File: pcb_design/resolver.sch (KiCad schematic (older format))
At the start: 37 parts, among them U15 AD2S1205, U18 SN74LVC1G, U19 AD8397, U20 APX809, U21 NCV78Mxx, X1 ABM3B - 8MHz

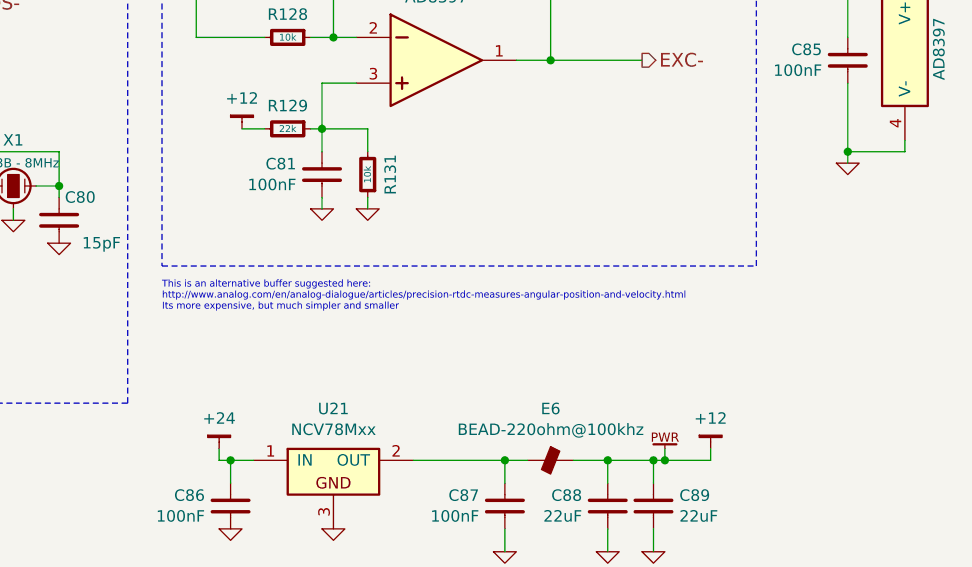
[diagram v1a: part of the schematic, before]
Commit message: Added RC filter to FAULT line to prevent noise triggering it
Signed-off-by: Marcos Chaparro <mchaparro@paltatech.com>
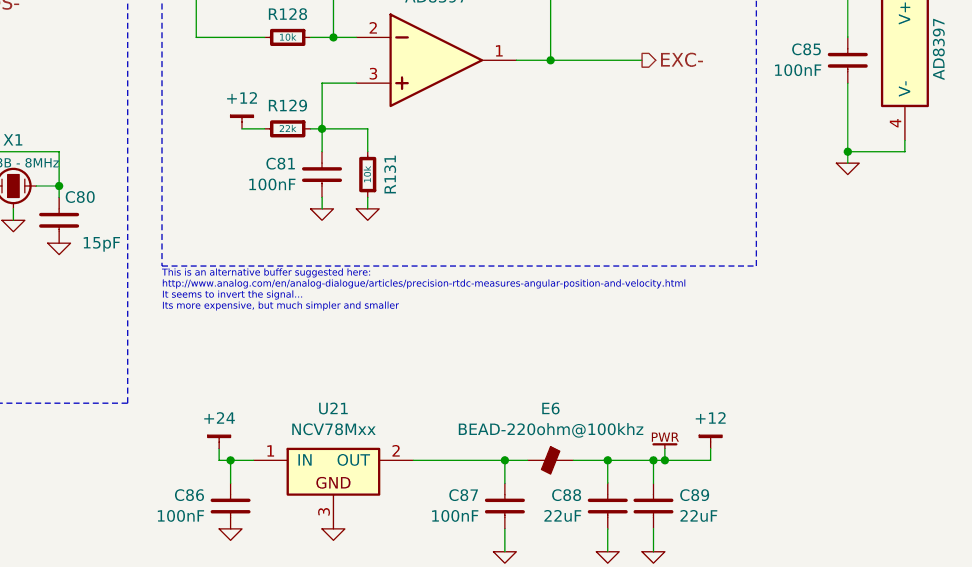
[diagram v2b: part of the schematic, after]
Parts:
- C73, C74, C75, C77, C81, C82, C85, C86, C87: BOM CAP MLCC 100pF C0G 50V 5% [0603] -> CAP MLCC 100nF C0G 50V 5% [0603]
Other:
- note added: "This is an alternative buffer suggested here:\nhttp://www.analog.com/en/analog-dialogue/articles/precision-rtdc-measures-angular-position-and-velocity.html\nIt seems to invert the signal...\nIts more expensive, but much simpler and smaller"
- note removed: "This is an alternative buffer suggested here:\nhttp://www.analog.com/en/analog-dialogue/articles/precision-rtdc-measures-angular-position-and-velocity.html\nIts more expensive, but much simpler and smaller"
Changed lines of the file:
@@
 $Descr A4 11693 8268
 encoding utf-8
-Sheet 14 15
+Sheet 12 15
 Title ""
 Date "2017-02-22"
@@
 F 2 "IPC7351-Nominal:CAPC1608X55" H -50 -550 50  0001 C CNN
 F 3 "http://www.murata.com/~/media/webrenewal/support/library/catalog/products/capacitor/mlcc/c02e.ashx" H -60 -575 60  0001 C CNN
-F 4 "CAP MLCC 100pF C0G 50V 5% [0603]" H 750 0   60  0001 C CNN "BOM"
+F 4 "CAP MLCC 100nF C0G 50V 5% [0603]" H 750 0   60  0001 C CNN "BOM"
 F 5 "Murata Electronics North America" H 0   0   50  0001 C CNN "MFR"
 F 6 "GRM188R71E104KA01D" H 0   0   50  0001 C CNN "MPN"
@@
 F 2 "IPC7351-Nominal:CAPC1608X55" H -250 -550 50  0001 C CNN
 F 3 "http://www.murata.com/~/media/webrenewal/support/library/catalog/products/capacitor/mlcc/c02e.ashx" H -260 -575 60  0001 C CNN
-F 4 "CAP MLCC 100pF C0G 50V 5% [0603]" H 550 0   60  0001 C CNN "BOM"
+F 4 "CAP MLCC 100nF C0G 50V 5% [0603]" H 550 0   60  0001 C CNN "BOM"
 F 5 "Murata Electronics North America" H 0   0   50  0001 C CNN "MFR"
 F 6 "GRM188R71E104KA01D" H 0   0   50  0001 C CNN "MPN"
@@
 F 2 "IPC7351-Nominal:CAPC1608X55" H 1100 -400 50  0001 C CNN
 F 3 "http://www.murata.com/~/media/webrenewal/support/library/catalog/products/capacitor/mlcc/c02e.ashx" H 1090 -425 60  0001 C CNN
-F 4 "CAP MLCC 100pF C0G 50V 5% [0603]" H 1900 150 60  0001 C CNN "BOM"
+F 4 "CAP MLCC 100nF C0G 50V 5% [0603]" H 1900 150 60  0001 C CNN "BOM"
 F 5 "Murata Electronics North America" H 0   0   50  0001 C CNN "MFR"
 F 6 "GRM188R71E104KA01D" H 0   0   50  0001 C CNN "MPN"
@@
 F 2 "IPC7351-Nominal:CAPC1608X55" H 4000 500 50  0001 C CNN
 F 3 "http://www.murata.com/~/media/webrenewal/support/library/catalog/products/capacitor/mlcc/c02e.ashx" H 3990 475 60  0001 C CNN
-F 4 "CAP MLCC 100pF C0G 50V 5% [0603]" H 4800 1050 60  0001 C CNN "BOM"
+F 4 "CAP MLCC 100nF C0G 50V 5% [0603]" H 4800 1050 60  0001 C CNN "BOM"
 F 5 "Murata Electronics North America" H 0   0   50  0001 C CNN "MFR"
 F 6 "GRM188R71E104KA01D" H 0   0   50  0001 C CNN "MPN"
@@
 F 2 "IPC7351-Nominal:CAPC1608X55" H 3800 2250 50  0001 C CNN
 F 3 "http://www.murata.com/~/media/webrenewal/support/library/catalog/products/capacitor/mlcc/c02e.ashx" H 3790 2225 60  0001 C CNN
-F 4 "CAP MLCC 100pF C0G 50V 5% [0603]" H 4600 2800 60  0001 C CNN "BOM"
+F 4 "CAP MLCC 100nF C0G 50V 5% [0603]" H 4600 2800 60  0001 C CNN "BOM"
 F 5 "Murata Electronics North America" H 0   0   50  0001 C CNN "MFR"
 F 6 "GRM188R71E104KA01D" H 0   0   50  0001 C CNN "MPN"
@@
 F 2 "IPC7351-Nominal:CAPC1608X55" H 6100 1750 50  0001 C CNN
 F 3 "http://www.murata.com/~/media/webrenewal/support/library/catalog/products/capacitor/mlcc/c02e.ashx" H 6090 1725 60  0001 C CNN
-F 4 "CAP MLCC 100pF C0G 50V 5% [0603]" H 6900 2300 60  0001 C CNN "BOM"
+F 4 "CAP MLCC 100nF C0G 50V 5% [0603]" H 6900 2300 60  0001 C CNN "BOM"
 F 5 "Murata Electronics North America" H 0   0   50  0001 C CNN "MFR"
 F 6 "GRM188R71E104KA01D" H 0   0   50  0001 C CNN "MPN"
@@
 F 2 "IPC7351-Nominal:CAPC1608X55" H -2450 1750 50  0001 C CNN
 F 3 "http://www.murata.com/~/media/webrenewal/support/library/catalog/products/capacitor/mlcc/c02e.ashx" H -2460 1725 60  0001 C CNN
-F 4 "CAP MLCC 100pF C0G 50V 5% [0603]" H -1650 2300 60  0001 C CNN "BOM"
+F 4 "CAP MLCC 100nF C0G 50V 5% [0603]" H -1650 2300 60  0001 C CNN "BOM"
 F 5 "Murata Electronics North America" H 0   0   50  0001 C CNN "MFR"
 F 6 "GRM188R71E104KA01D" H 0   0   50  0001 C CNN "MPN"
@@
 F 2 "IPC7351-Nominal:CAPC1608X55" H 4600 3700 50  0001 C CNN
 F 3 "http://www.murata.com/~/media/webrenewal/support/library/catalog/products/capacitor/mlcc/c02e.ashx" H 4590 3675 60  0001 C CNN
-F 4 "CAP MLCC 100pF C0G 50V 5% [0603]" H 5400 4250 60  0001 C CNN "BOM"
+F 4 "CAP MLCC 100nF C0G 50V 5% [0603]" H 5400 4250 60  0001 C CNN "BOM"
 F 5 "Murata Electronics North America" H 0   0   50  0001 C CNN "MFR"
 F 6 "GRM188R71E104KA01D" H 0   0   50  0001 C CNN "MPN"
@@
 F 2 "IPC7351-Nominal:CAPC1608X55" H 3400 3700 50  0001 C CNN
 F 3 "http://www.murata.com/~/media/webrenewal/support/library/catalog/products/capacitor/mlcc/c02e.ashx" H 3390 3675 60  0001 C CNN
-F 4 "CAP MLCC 100pF C0G 50V 5% [0603]" H 4200 4250 60  0001 C CNN "BOM"
+F 4 "CAP MLCC 100nF C0G 50V 5% [0603]" H 4200 4250 60  0001 C CNN "BOM"
 F 5 "Murata Electronics North America" H 0   0   50  0001 C CNN "MFR"
 F 6 "GRM188R71E104KA01D" H 0   0   50  0001 C CNN "MPN"
@@
 Buffer
 Text Notes 7600 5550 0    30   ~ 0
-This is an alternative buffer suggested here:\nhttp://www.analog.com/en/analog-dialogue/articles/precision-rtdc-measures-angular-position-and-velocity.html\nIts more expensive, but much simpler and smaller
+This is an alternative buffer suggested here:\nhttp://www.analog.com/en/analog-dialogue/articles/precision-rtdc-measures-angular-position-and-velocity.html\nIt seems to invert the signal...\nIts more expensive, but much simpler and smaller
 Text Notes 2900 2900 0    40   ~ 0
 RESET line requires\na voltage monitor
